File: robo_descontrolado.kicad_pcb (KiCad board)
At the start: 2 copper layers, 80 x 100 mm, 20 parts, among them J1 Bus_PCI_microbit, J10 Conn_01x05, J11 Conn_01x05, J2 Jack_Switch, J3 Screw_Terminal, J4 RJ45, J5 RJ45, J6 Conn_01x02, J7 Conn_01x05, J8 Conn_01x02, J9 Conn_01x02, SW1 SW_SPDT, SW2 SW_SPST, U1 TB6612FNG_modulo, U3 LM1117-3.3

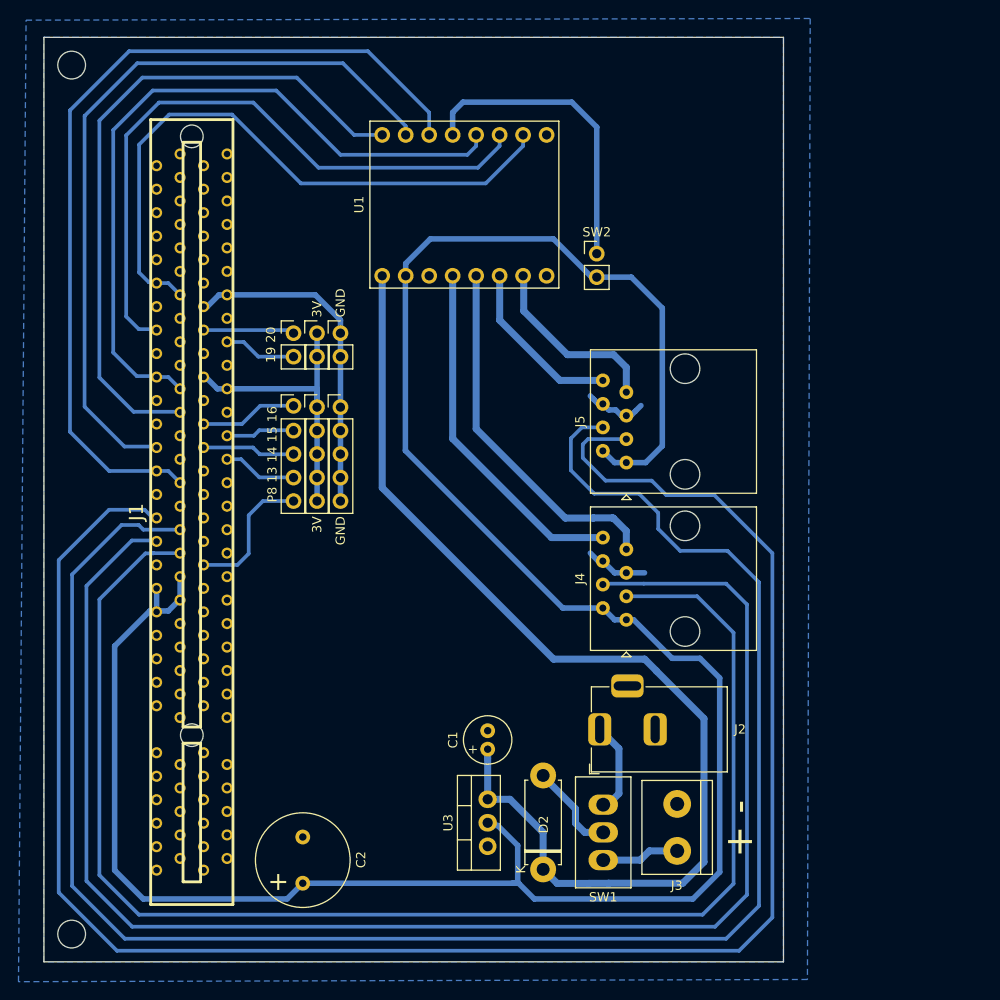
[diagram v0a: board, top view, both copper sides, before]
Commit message: Nova versão com expansor i2c e IOs de propósito geral
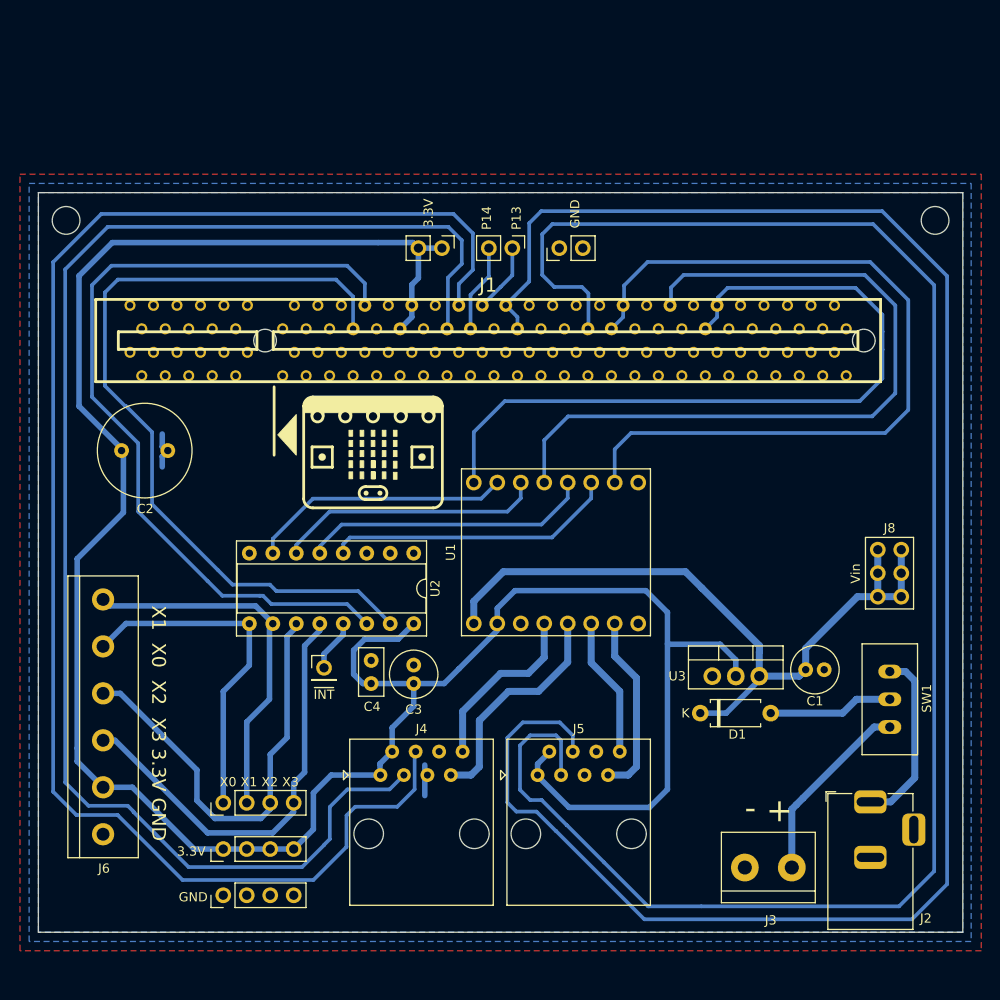
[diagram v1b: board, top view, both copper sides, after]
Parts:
- removed D2: D, Diode_THT:D_5W_P10.16mm_Horizontal
- removed the REF** at (104.6, 47.2)
- removed the REF** at (104.6, 138.7)
- removed SW2: SW_SPST, Connector_PinHeader_2.54mm:PinHeader_1x02_P2.54mm_Vertical
- added C3: 10uF, robo_descontrolado:C_Radial_D5.0mm_H11.0mm_P2.00mm, F.Cu at (140.6, 113.1)
- added C4: 100nF, robo_descontrolado:C_Disc_D5.0mm_W2.5mm_P2.50mm, F.Cu at (136.0, 110.6)
- added D1: 1N5817, robo_descontrolado:D_A-405_P7.62mm_Horizontal, F.Cu at (171.6, 116.3)
- added G***: LOGO, robo_descontrolado:microbit-icon, F.Cu at (136.2, 88.6)
- added J12: Conn_01x02_Male, robo_descontrolado:PinHeader_1x02_P2.54mm_Vertical, F.Cu at (156.3, 66.0)
- added J13: Conn_01x02_Male, robo_descontrolado:PinHeader_1x02_P2.54mm_Vertical, F.Cu at (151.3, 66.0)
- added J14: Conn_01x01_Male, robo_descontrolado:PinHeader_1x01_P2.54mm_Vertical, F.Cu at (130.9, 111.4)
- added REF**: MountingHole_3.2mm_M3, MountingHole:MountingHole_3.2mm_M3, F.Cu at (104.5, 64.0)
- added REF**: MountingHole_3.2mm_M3, MountingHole:MountingHole_3.2mm_M3, F.Cu at (196.0, 64.0)
- added U2: PCF8574, robo_descontrolado:DIP-16_W7.62mm_Socket, F.Cu at (140.6, 99.0)
- C1: value C -> 10uF; footprint Capacitor_THT:C_Radial_D5.0mm_H11.0mm_P2.00mm -> robo_descontrolado:C_Radial_D5.0mm_H11.0mm_P2.00mm
- C2: value C -> 2200uF; footprint Capacitor_THT:C_Radial_D10.0mm_H16.0mm_P5.00mm -> robo_descontrolado:C_Radial_D10.0mm_H16.0mm_P5.00mm
- J1: footprint Personal:pci_connector_microbit -> robo_descontrolado:pci_connector_microbit
- J10, J7: value Conn_01x05 -> Conn_01x04_Male; footprint Connector_PinHeader_2.54mm:PinHeader_1x05_P2.54mm_Vertical -> robo_descontrolado:PinHeader_1x04_P2.54mm_Vertical
- J11: value Conn_01x05 -> Conn_01x02_Male; footprint Connector_PinHeader_2.54mm:PinHeader_1x05_P2.54mm_Vertical -> robo_descontrolado:PinHeader_1x02_P2.54mm_Vertical
- J2: value Jack_Switch -> Jack_P4; footprint Connector_BarrelJack:BarrelJack_Horizontal -> robo_descontrolado:BarrelJack_Horizontal
- J3: value Screw_Terminal -> KRE; footprint TerminalBlock:TerminalBlock_bornier-2_P5.08mm -> robo_descontrolado:TerminalBlock_bornier-2_P5.08mm
- J4, J5: footprint Connector_RJ:RJ45_Amphenol_54602-x08_Horizontal -> robo_descontrolado:RJ45_Amphenol_54602-x08_Horizontal
- J6: value Conn_01x02 -> Screw_Terminal_01x06; footprint Connector_PinHeader_2.54mm:PinHeader_1x02_P2.54mm_Vertical -> robo_descontrolado:TerminalBlock_bornier-6_P5.08mm
- J8: value Conn_01x02 -> Conn_01x05_Male; footprint Connector_PinHeader_2.54mm:PinHeader_1x02_P2.54mm_Vertical -> robo_descontrolado:PinHeader_2x03_P2.54mm_Vertical
- J9: value Conn_01x02 -> Conn_01x04_Male; footprint Connector_PinHeader_2.54mm:PinHeader_1x02_P2.54mm_Vertical -> robo_descontrolado:PinHeader_1x04_P2.54mm_Vertical
- SW1: footprint Personal:Slide_Switch -> robo_descontrolado:Slide_Switch
- U1: footprint Personal:TB6612FNG_modulo -> robo_descontrolado:TB6612FNG_modulo
- U3: footprint Package_TO_SOT_THT:TO-220-3_Vertical -> robo_descontrolado:TO-220-3_Vertical
- moved J8 62.7 mm to (190.8, 98.6)
- moved J10 53.3 mm to (120.0, 136.0), turned to 90 degrees
- moved J9 51.8 mm to (120.0, 126.0), turned to 90 degrees
- moved C2 50.7 mm to (109.0, 87.9), turned to 0 degrees
- moved J7 49.5 mm to (120.0, 131.0), turned to 90 degrees
- moved U1 38.9 mm to (147.1, 106.6)
- moved J1 37.0 mm to (148.7, 76.0), turned to 0 degrees
- moved C1 35.5 mm to (183.0, 111.6), turned to 0 degrees
- moved J6 35.4 mm to (107.0, 104.0), turned to -90 degrees
- moved J5 35.1 mm to (154.0, 123.0), turned to 0 degrees
- moved SW1 34.2 mm to (192.1, 111.8)
- moved J4 31.5 mm to (137.0, 123.0), turned to 0 degrees
- moved U3 30.5 mm to (172.9, 112.3), turned to 0 degrees
- moved J2 30.3 mm to (190.0, 125.9), turned to 90 degrees
- moved J11 21.9 mm to (143.7, 66.0), turned to -90 degrees
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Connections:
- net MA1 renamed /AO1
- net MA2 renamed /AO2
- net MB1 renamed /BO1
- net MB2 renamed /BO2
- net Net-(J1-PadB24) renamed /P9
- net SENA1 renamed /ENCA2
- net SENA2 renamed /ENCA1
- C1 pad 1: +Vin -> VD
- J1 pad A1: Net-(J1-PadA1) -> unconnected-(J1-PadA1)
- J1 pad A10: Net-(J1-PadA10) -> unconnected-(J1-PadA10)
- J1 pad A11: Net-(J1-PadA11) -> unconnected-(J1-PadA11)
- J1 pad A12: Net-(J1-PadA11) -> unconnected-(J1-PadA12)
- J1 pad A13: Net-(J1-PadA11) -> unconnected-(J1-PadA13)
- J1 pad A14: Net-(J1-PadA11) -> unconnected-(J1-PadA14)
- J1 pad A15: Net-(J1-PadA15) -> unconnected-(J1-PadA15)
- J1 pad A16: Net-(J1-PadA16) -> unconnected-(J1-PadA16)
- J1 pad A17: Net-(J1-PadA17) -> unconnected-(J1-PadA17)
- J1 pad A18: Net-(J1-PadA18) -> unconnected-(J1-PadA18)
- J1 pad A19: Net-(J1-PadA19) -> unconnected-(J1-PadA19)
- J1 pad A2: Net-(J1-PadA2) -> unconnected-(J1-PadA2)
- J1 pad A20: Net-(J1-PadA19) -> unconnected-(J1-PadA20)
- J1 pad A21: Net-(J1-PadA19) -> unconnected-(J1-PadA21)
- J1 pad A22: Net-(J1-PadA19) -> unconnected-(J1-PadA22)
- J1 pad A23: Net-(J1-PadA23) -> unconnected-(J1-PadA23)
- J1 pad A24: Net-(J1-PadA24) -> unconnected-(J1-PadA24)
- J1 pad A25: Net-(J1-PadA25) -> unconnected-(J1-PadA25)
- J1 pad A26: Net-(J1-PadA26) -> unconnected-(J1-PadA26)
- J1 pad A27: Net-(J1-PadA27) -> unconnected-(J1-PadA27)
- J1 pad A28: Net-(J1-PadA28) -> unconnected-(J1-PadA28)
- J1 pad A29: Net-(J1-PadA29) -> unconnected-(J1-PadA29)
- J1 pad A3: Net-(J1-PadA3) -> unconnected-(J1-PadA3)
- J1 pad A30: Net-(J1-PadA30) -> unconnected-(J1-PadA30)
- J1 pad A31: Net-(J1-PadA31) -> unconnected-(J1-PadA31)
- J1 pad A32: Net-(J1-PadA32) -> unconnected-(J1-PadA32)
- J1 pad A33: Net-(J1-PadA33) -> unconnected-(J1-PadA33)
- J1 pad A34: Net-(J1-PadA34) -> unconnected-(J1-PadA34)
- J1 pad A35: Net-(J1-PadA35) -> unconnected-(J1-PadA35)
- J1 pad A36: Net-(J1-PadA36) -> unconnected-(J1-PadA36)
- J1 pad A37: Net-(J1-PadA37) -> unconnected-(J1-PadA37)
- J1 pad A38: Net-(J1-PadA38) -> unconnected-(J1-PadA38)
- J1 pad A39: Net-(J1-PadA39) -> unconnected-(J1-PadA39)
- J1 pad A4: Net-(J1-PadA4) -> unconnected-(J1-PadA4)
- J1 pad A40: Net-(J1-PadA40) -> unconnected-(J1-PadA40)
- J1 pad A41: Net-(J1-PadA41) -> unconnected-(J1-PadA41)
- J1 pad A42: Net-(J1-PadA42) -> unconnected-(J1-PadA42)
- J1 pad A43: Net-(J1-PadA43) -> unconnected-(J1-PadA43)
- J1 pad A44: Net-(J1-PadA44) -> unconnected-(J1-PadA44)
- J1 pad A45: Net-(J1-PadA45) -> unconnected-(J1-PadA45)
- J1 pad A46: Net-(J1-PadA46) -> unconnected-(J1-PadA46)
- J1 pad A47: Net-(J1-PadA47) -> unconnected-(J1-PadA47)
- J1 pad A48: Net-(J1-PadA48) -> unconnected-(J1-PadA48)
- J1 pad A49: Net-(J1-PadA49) -> unconnected-(J1-PadA49)
- J1 pad A5: Net-(J1-PadA5) -> unconnected-(J1-PadA5)
- J1 pad A52: Net-(J1-PadA52) -> unconnected-(J1-PadA52)
- J1 pad A53: Net-(J1-PadA53) -> unconnected-(J1-PadA53)
- J1 pad A54: Net-(J1-PadA54) -> unconnected-(J1-PadA54)
- J1 pad A55: Net-(J1-PadA55) -> unconnected-(J1-PadA55)
- J1 pad A56: Net-(J1-PadA56) -> unconnected-(J1-PadA56)
- J1 pad A57: Net-(J1-PadA57) -> unconnected-(J1-PadA57)
- J1 pad A58: Net-(J1-PadA58) -> unconnected-(J1-PadA58)
- J1 pad A59: Net-(J1-PadA59) -> unconnected-(J1-PadA59)
- J1 pad A6: Net-(J1-PadA6) -> unconnected-(J1-PadA6)
- J1 pad A60: Net-(J1-PadA60) -> unconnected-(J1-PadA60)
- J1 pad A61: Net-(J1-PadA61) -> unconnected-(J1-PadA61)
- J1 pad A62: Net-(J1-PadA62) -> unconnected-(J1-PadA62)
- J1 pad A7: Net-(J1-PadA7) -> unconnected-(J1-PadA7)
- J1 pad A8: Net-(J1-PadA8) -> unconnected-(J1-PadA8)
- J1 pad A9: Net-(J1-PadA9) -> unconnected-(J1-PadA9)
- J1 pad B1: Net-(J1-PadB1) -> unconnected-(J1-PadB1)
- J1 pad B10: Net-(J1-PadB10) -> unconnected-(J1-PadB10)
- J1 pad B11: PWMB -> unconnected-(J1-PadB11)
- J1 pad B12: PWMB -> /PWMA
- J1 pad B13: PWMB -> /PWMA
- J1 pad B14: PWMB -> unconnected-(J1-PadB14)
- J1 pad B15: Net-(J1-PadB15) -> unconnected-(J1-PadB15)
- J1 pad B16: BIN2 -> /STBY
- J1 pad B17: Net-(J1-PadB17) -> unconnected-(J1-PadB17)
- J1 pad B18: Net-(J1-PadB18) -> unconnected-(J1-PadB18)
- J1 pad B19: BIN1 -> unconnected-(J1-PadB19)
- J1 pad B2: Net-(J1-PadB2) -> unconnected-(J1-PadB2)
- J1 pad B20: BIN1 -> /PWMB
- J1 pad B21: BIN1 -> /PWMB
- J1 pad B22: BIN1 -> unconnected-(J1-PadB22)
- J1 pad B23: PWMA -> /ENCB2
- J1 pad B25: Net-(J1-PadB25) -> unconnected-(J1-PadB25)
- J1 pad B26: AIN2 -> unconnected-(J1-PadB26)
- J1 pad B27: Net-(J1-PadB27) -> unconnected-(J1-PadB27)
- J1 pad B28: AIN1 -> unconnected-(J1-PadB28)
- J1 pad B29: AIN1 -> /ENCB1
- J1 pad B3: Net-(J1-PadB3) -> unconnected-(J1-PadB3)
- J1 pad B30: AIN1 -> /ENCB1
- J1 pad B31: AIN1 -> unconnected-(J1-PadB31)
- J1 pad B32: SENB2 -> /P13
- J1 pad B33: SENB1 -> /P14
- J1 pad B36: Net-(J1-PadB36) -> unconnected-(J1-PadB36)
- J1 pad B37: +3.3V -> unconnected-(J1-PadB37)
- J1 pad B4: Net-(J1-PadB4) -> unconnected-(J1-PadB4)
- J1 pad B40: +3.3V -> unconnected-(J1-PadB40)
- J1 pad B41: Net-(J1-PadB41) -> unconnected-(J1-PadB41)
- J1 pad B42: Net-(J1-PadB42) -> /SCL
- J1 pad B43: Net-(J1-PadB43) -> /SDA
- J1 pad B44: Net-(J1-PadB44) -> unconnected-(J1-PadB44)
- J1 pad B49: Net-(J1-PadB49) -> unconnected-(J1-PadB49)
- J1 pad B5: Net-(J1-PadB5) -> unconnected-(J1-PadB5)
- J1 pad B52: Net-(J1-PadB52) -> unconnected-(J1-PadB52)
- J1 pad B53: Net-(J1-PadB53) -> unconnected-(J1-PadB53)
- J1 pad B54: Net-(J1-PadB54) -> unconnected-(J1-PadB54)
- J1 pad B55: Net-(J1-PadB55) -> unconnected-(J1-PadB55)
- J1 pad B56: Net-(J1-PadB56) -> unconnected-(J1-PadB56)
- J1 pad B57: Net-(J1-PadB57) -> unconnected-(J1-PadB57)
- J1 pad B58: Net-(J1-PadB58) -> unconnected-(J1-PadB58)
- J1 pad B59: Net-(J1-PadB59) -> unconnected-(J1-PadB59)
- J1 pad B6: Net-(J1-PadB6) -> unconnected-(J1-PadB6)
- J1 pad B60: Net-(J1-PadB60) -> unconnected-(J1-PadB60)
- J1 pad B61: Net-(J1-PadB61) -> unconnected-(J1-PadB61)
- J1 pad B62: Net-(J1-PadB62) -> unconnected-(J1-PadB62)
- J1 pad B7: Net-(J1-PadB7) -> unconnected-(J1-PadB7)
- J1 pad B8: Net-(J1-PadB8) -> unconnected-(J1-PadB8)
- J1 pad B9: Net-(J1-PadB9) -> unconnected-(J1-PadB9)
- J10 pad 1: Net-(J1-PadA24) -> GND
- J10 pad 2: Net-(J1-PadA25) -> GND
- J10 pad 3: Net-(J1-PadA26) -> GND
- J10 pad 4: Net-(J1-PadA27) -> GND
- J11 pad 1: Net-(J1-PadA19) -> +3.3V
- J11 pad 2: Net-(J1-PadA19) -> +3.3V
- J3 pad 1: Net-(J3-Pad1) -> GND
- J3 pad 2: GND -> Net-(J3-Pad2)
- J5 pad 3: SENB2 -> /ENCB2
- J5 pad 4: SENB1 -> /ENCB1
- J6 pad 1: Net-(J1-PadA16) -> /X1
- J6 pad 2: Net-(J1-PadA17) -> /X0
- J7 pad 1: Net-(J1-PadA11) -> +3.3V
- J7 pad 2: Net-(J1-PadA11) -> +3.3V
- J7 pad 3: Net-(J1-PadA11) -> +3.3V
- J7 pad 4: Net-(J1-PadA11) -> +3.3V
- J8 pad 1: Net-(J1-PadA11) -> VD
- J8 pad 2: Net-(J1-PadA11) -> VD
- J9 pad 1: Net-(J1-PadA19) -> /X0
- J9 pad 2: Net-(J1-PadA19) -> /X1
- SW1 pad 3: Net-(J3-Pad1) -> Net-(J3-Pad2)
- U1 pad 1: +Vin -> VD
- U1 pad 10: PWMB -> /PWMB
- U1 pad 11: BIN2 -> /BIN2
- U1 pad 12: BIN1 -> /BIN1
- U1 pad 13: Net-(SW2-Pad1) -> /STBY
- U1 pad 14: AIN1 -> /AIN1
- U1 pad 15: AIN2 -> /AIN2
- U1 pad 16: PWMA -> /PWMA
- U3 pad 3: +Vin -> VD
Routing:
- net SENB2: track 201.1 -> 0.00 mm
- net /ENCB1: track 0.00 -> 198.9 mm
- net SENB1: track 194.7 -> 0.00 mm
- net /ENCB2: track 0.00 -> 188.3 mm
- net +Vin: track 119.3 -> 0.00 mm
- net AIN1: track 95.6 -> 0.00 mm
- net /SCL: track 0.00 -> 89.9 mm
- net /SDA: track 0.00 -> 87.8 mm
- net /PWMB: track 0.00 -> 87.7 mm
- net /PWMA: track 0.00 -> 82.3 mm
- net /STBY: track 0.00 -> 82.3 mm
- net AIN2: track 81.9 -> 0.00 mm
- net VD: track 0.00 -> 80.0 mm
- net BIN1: track 78.4 -> 0.00 mm
- net PWMA: track 73.2 -> 0.00 mm
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- added copper zone on F.Cu, net GND
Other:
- board size 80 x 100 mm -> 100 x 80 mm
- net class Default removed
- net class Motor removed
- net class Power removed
- net class Signal removed
- net class teste1 removed
- board text added: "3.3V"
- board text added: "P14 P13"
- board text added: "Vin"
- board text added: "X0 X1 X2 X3"
- board text added: "X1 X0 X2 X3 3.3V GND"
- board text added: "~{INT}"
- board text removed: "+"
- board text removed: "19 20"
- board text removed: "3V"
- board text removed: "P8 13 14 15 16"
